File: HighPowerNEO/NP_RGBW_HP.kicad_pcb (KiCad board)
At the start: 2 copper layers, 81 x 40 mm, 45 parts, among them J1 Conn_01x03, J2 Conn_01x03, Q1 S8550, Q2 S8550, Q3 S8550, Q4 S8550, U1 UCS2904B

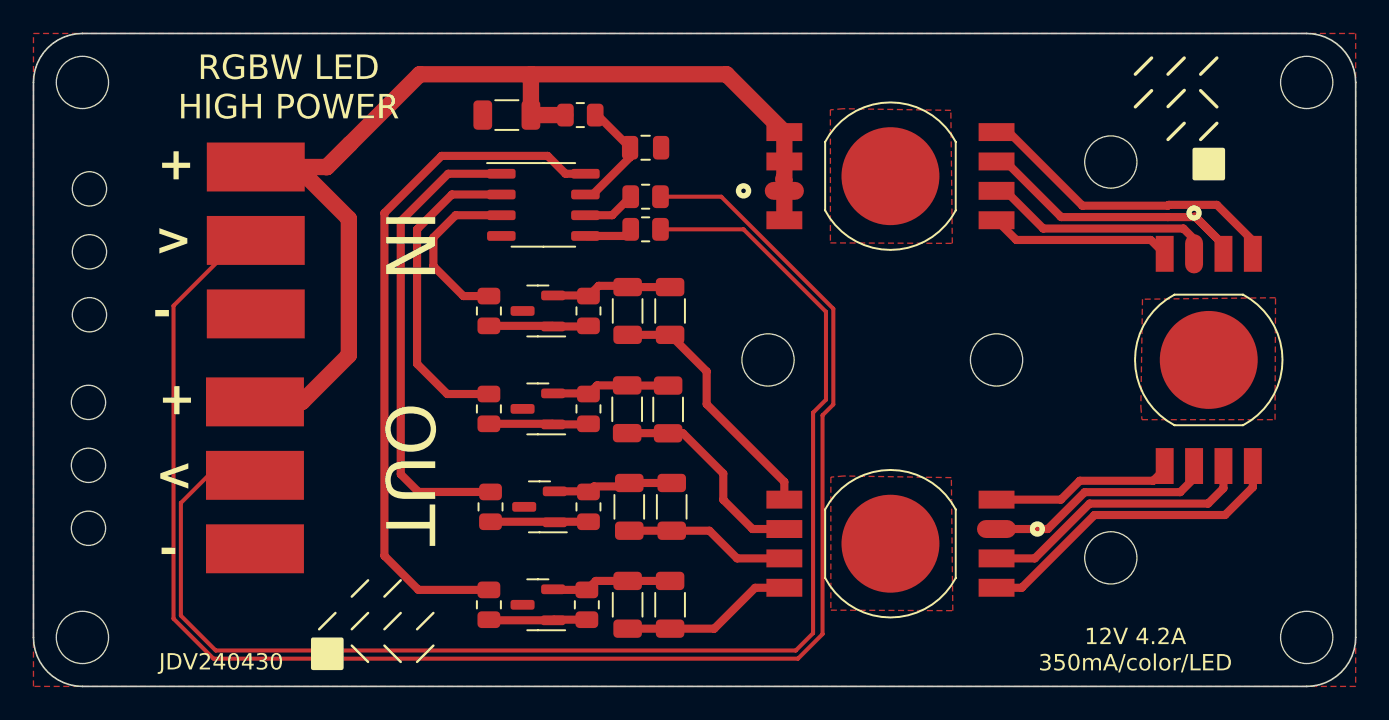
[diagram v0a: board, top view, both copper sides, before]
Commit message: silkscreen for radar sensor, more code examples, better readme
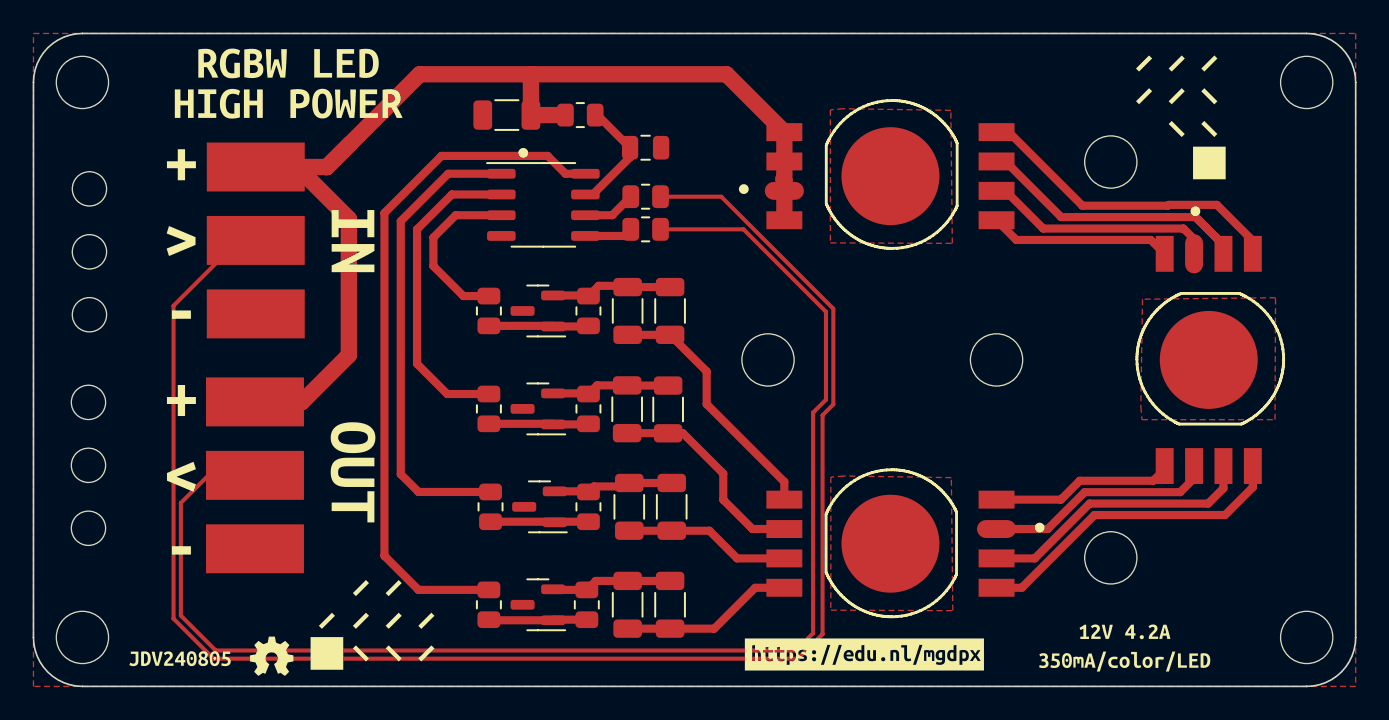
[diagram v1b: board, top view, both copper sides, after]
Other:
- board text removed: "+"
- board text removed: "-"
- board text removed: "12V 4.2A 350mA/color/LED"
- board text removed: "<"
- board text removed: ">"
- board text removed: "IN"
- board text removed: "JDV240430"
- board text removed: "OUT"
- board text removed: "RGBW LED HIGH POWER"
